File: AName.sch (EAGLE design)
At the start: 10 parts, among them IC1 LM555D

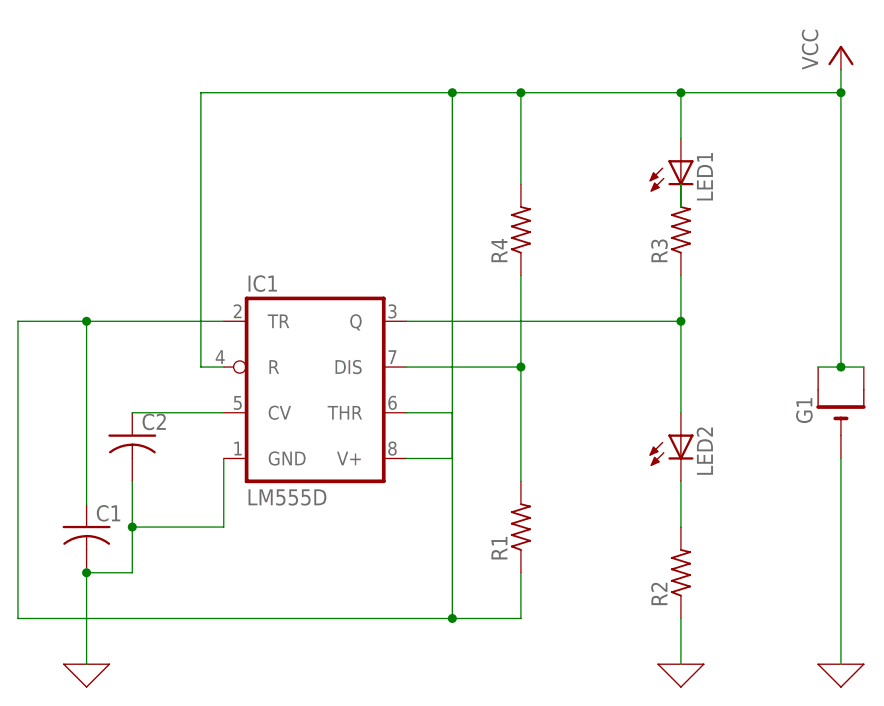
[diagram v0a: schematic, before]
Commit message: TH was wired to VDD. Fixed ERC errors.
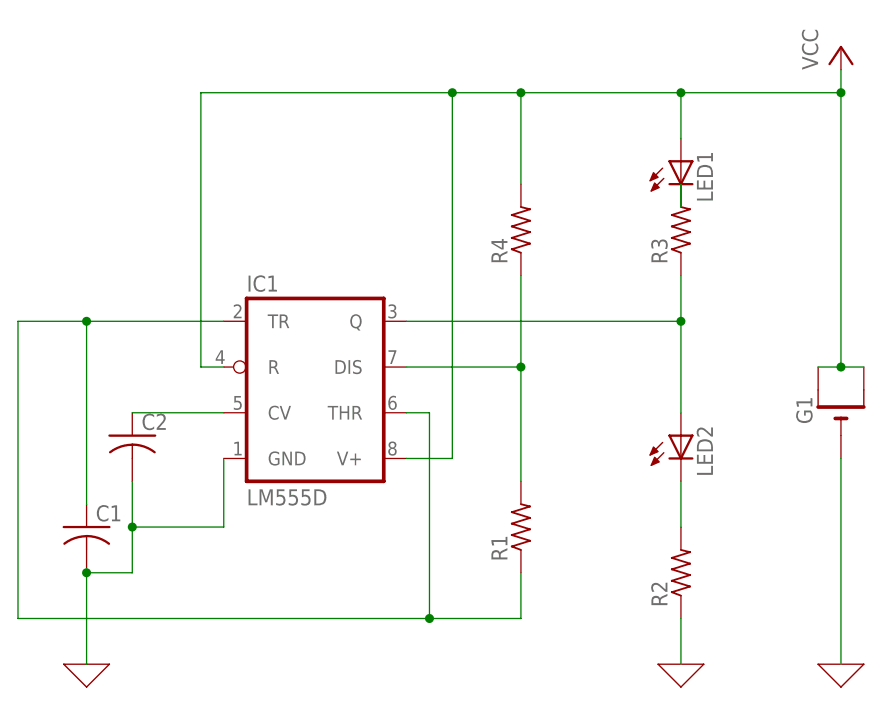
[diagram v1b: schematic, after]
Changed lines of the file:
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@@
 <wire x1="15.24" y1="53.34" x2="15.24" y2="20.32" width="0.1524" layer="91"/>
 <junction x="22.86" y="53.34"/>
+<pinref part="R1" gate="G$1" pin="1"/>
+<wire x1="71.12" y1="20.32" x2="71.12" y2="25.4" width="0.1524" layer="91"/>
+<wire x1="15.24" y1="20.32" x2="60.96" y2="20.32" width="0.1524" layer="91"/>
 <pinref part="IC1" gate="A" pin="THR"/>
-<wire x1="58.42" y1="43.18" x2="63.5" y2="43.18" width="0.1524" layer="91"/>
-<wire x1="63.5" y1="43.18" x2="63.5" y2="20.32" width="0.1524" layer="91"/>
-<pinref part="R1" gate="G$1" pin="1"/>
-<wire x1="63.5" y1="20.32" x2="71.12" y2="20.32" width="0.1524" layer="91"/>
-<wire x1="71.12" y1="20.32" x2="71.12" y2="25.4" width="0.1524" layer="91"/>
-<wire x1="15.24" y1="20.32" x2="63.5" y2="20.32" width="0.1524" layer="91"/>
-<junction x="63.5" y="20.32"/>
+<wire x1="60.96" y1="20.32" x2="71.12" y2="20.32" width="0.1524" layer="91"/>
+<wire x1="58.42" y1="43.18" x2="60.96" y2="43.18" width="0.1524" layer="91"/>
+<wire x1="60.96" y1="43.18" x2="60.96" y2="20.32" width="0.1524" layer="91"/>
+<junction x="60.96" y="20.32"/>
 </segment>
 </net>
@@
 </sheet>
 </sheets>
+<errors>
+</errors>
 </schematic>
 </drawing>
